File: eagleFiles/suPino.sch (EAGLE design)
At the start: 25 parts

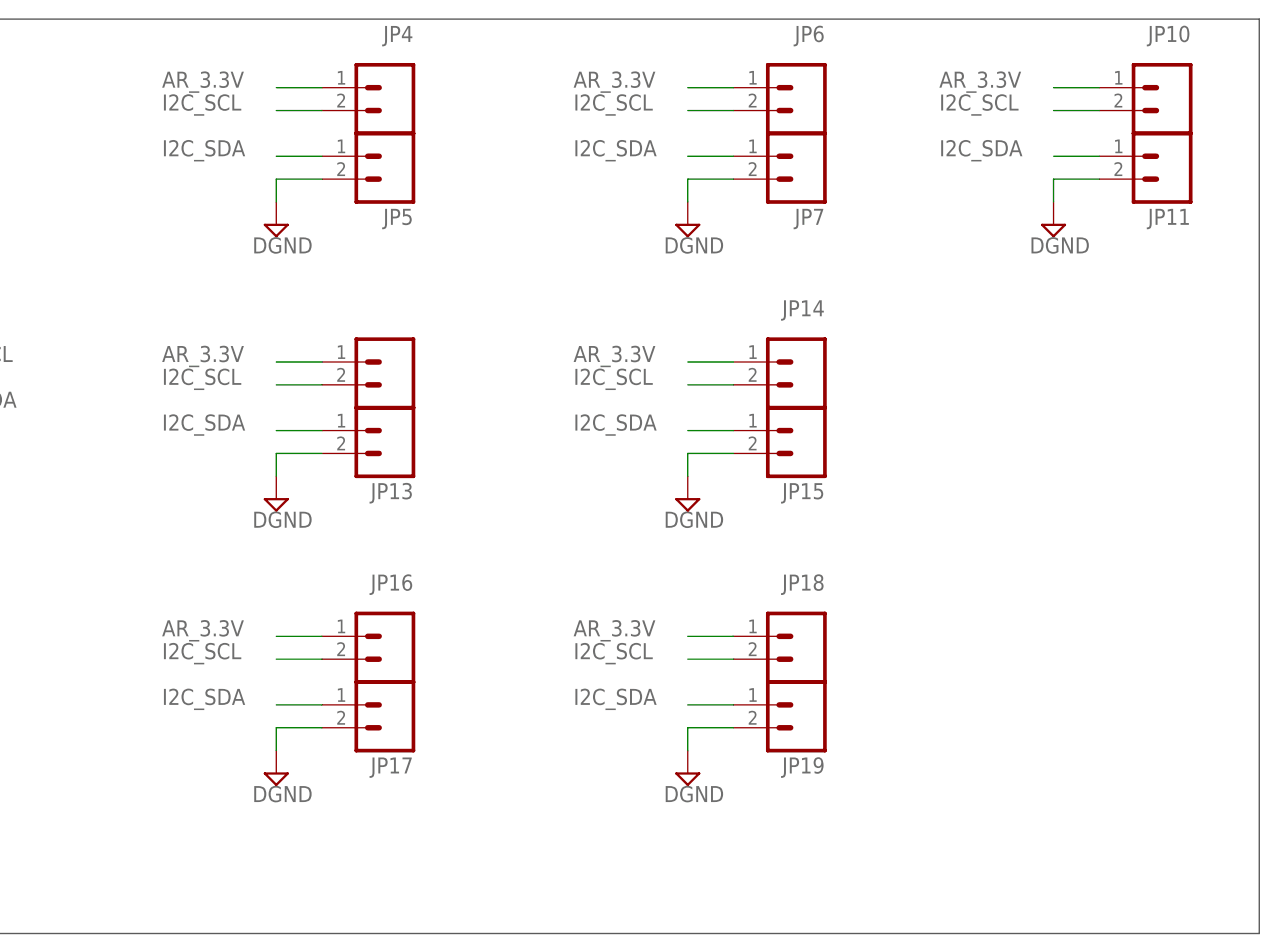
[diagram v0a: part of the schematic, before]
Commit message: Fixed the routing and added silkscreen
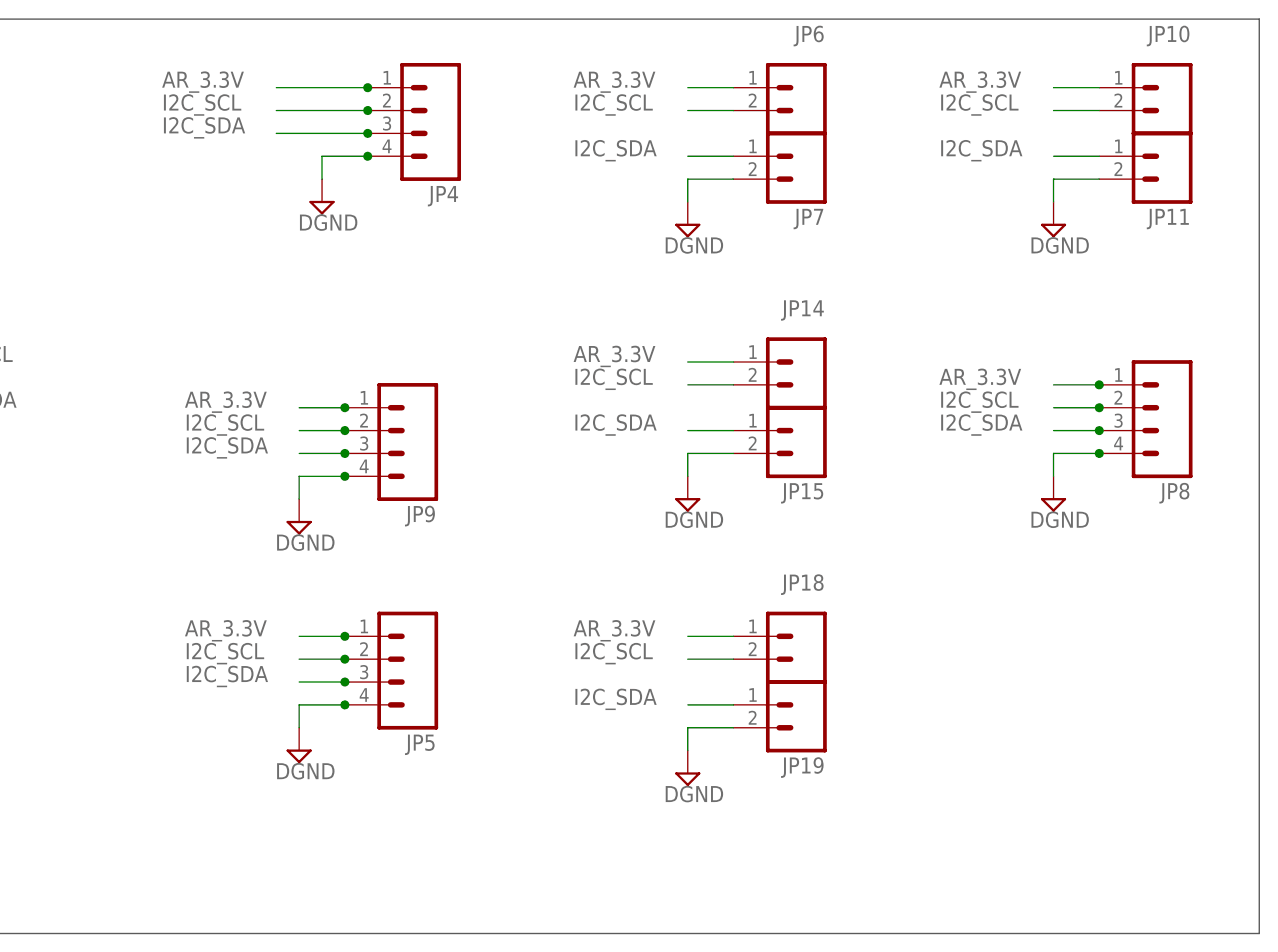
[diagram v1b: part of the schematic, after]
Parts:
- removed JP12, JP13, JP16, JP17: M023.5MM, SparkFun-Connectors:M023.5MM
- added JP8, JP9: (no value), SparkFun-Connectors:M04PTH
- JP4, JP5: value M023.5MM -> (none); device SparkFun-Connectors:M023.5MM -> SparkFun-Connectors:M04PTH
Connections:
- net AR_3.3V: now also JP5.1, JP8.1, JP9.1; no longer JP12.1, JP16.1
- net DGND: now also JP4.4, JP5.4, JP8.4, JP9.4; no longer JP13.2, JP17.2, JP5.2
- net I2C_SCL: now also JP5.2, JP8.2, JP9.2; no longer JP12.2, JP16.2
- net I2C_SDA: now also JP4.3, JP5.3, JP8.3, JP9.3; no longer JP13.1, JP17.1, JP5.1
